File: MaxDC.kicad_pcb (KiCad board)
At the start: 2 copper layers, 100 x 100 mm, 34 parts, among them J1 Screw_Terminal_01x03, J2 Screw_Terminal_01x04, T2 70063K

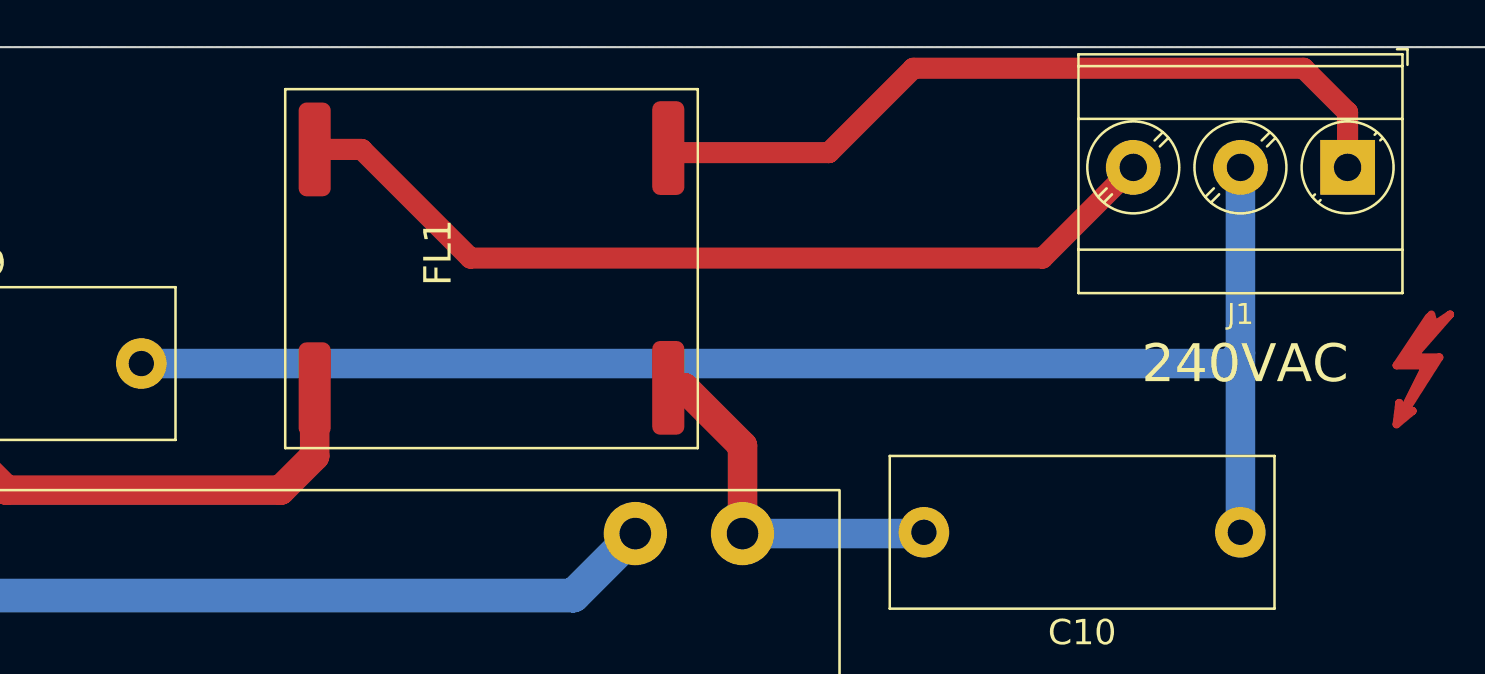
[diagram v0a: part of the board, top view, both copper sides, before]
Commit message: Add files via upload
Begin Changes for creepage.   Reverse N and E input terminals.
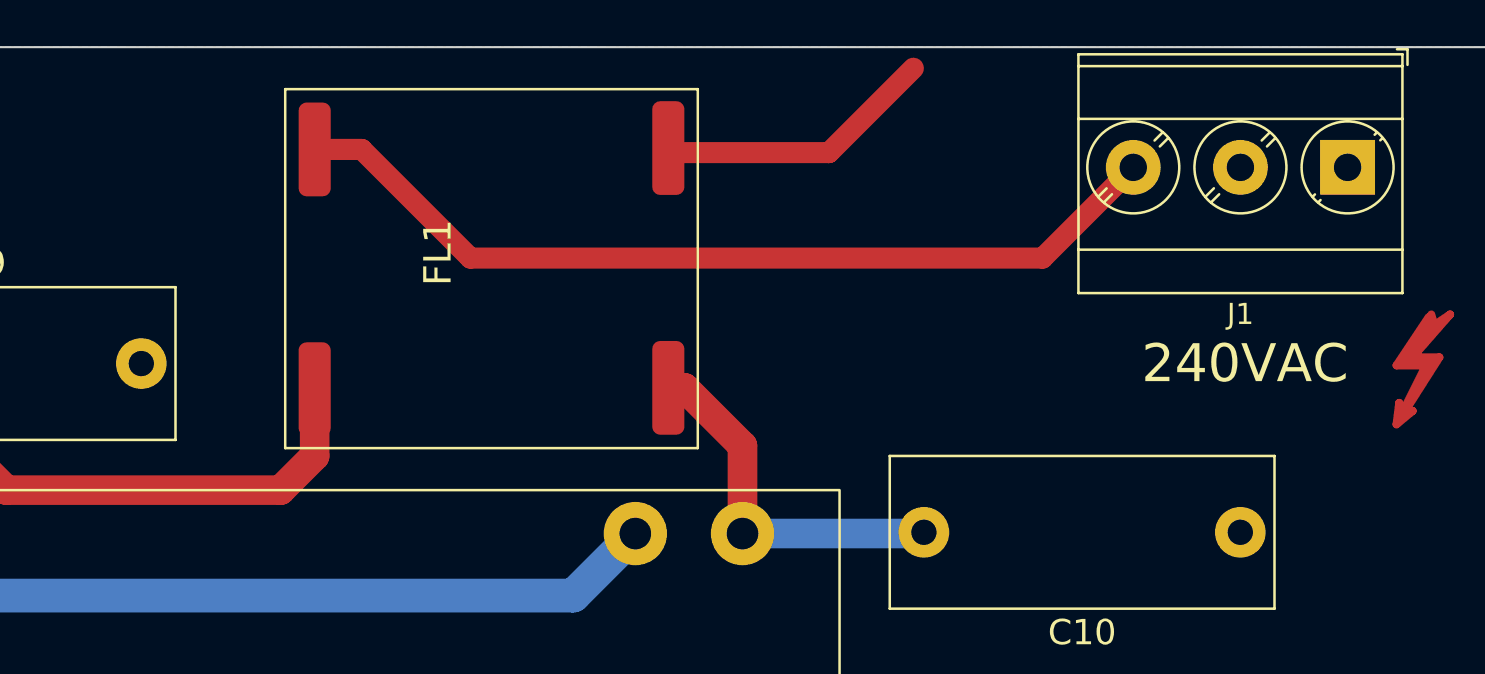
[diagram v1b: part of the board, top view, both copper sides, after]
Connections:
- J1 pad 1: Net-(FL1-Pad4) -> Earth_Protective
- J1 pad 2: Earth_Protective -> Net-(FL1-Pad4)
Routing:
- net Earth_Protective: track 69.6 -> 0.01 mm
- net Net-(FL1-Pad4): track 37.4 -> 13.4 mm
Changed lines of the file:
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@@
     (fp_circle (center 0 0) (end 2 0) (layer "F.Fab") (width 0.1) (fill none))
     (pad "1" thru_hole rect (at 0 0 180) (size 2.6 2.6) (drill 1.3) (layers *.Cu *.Mask)
-      (net 6 "Net-(FL1-Pad4)") (pinfunction "Pin_1") (pintype "passive"))
+      (net 7 "Earth_Protective") (pinfunction "Pin_1") (pintype "passive"))
     (pad "2" thru_hole circle (at 5.08 0 180) (size 2.6 2.6) (drill 1.3) (layers *.Cu *.Mask)
-      (net 7 "Earth_Protective") (pinfunction "Pin_2") (pintype "passive"))
+      (net 6 "Net-(FL1-Pad4)") (pinfunction "Pin_2") (pintype "passive"))
     (pad "3" thru_hole circle (at 10.16 0 180) (size 2.6 2.6) (drill 1.3) (layers *.Cu *.Mask)
       (net 8 "Net-(FL1-Pad1)") (pinfunction "Pin_3") (pintype "passive"))
@@
   (segment (start 105.1 73.06) (end 105.1 67.9) (width 1.4) (layer "B.Cu") (net 5))
   (segment (start 105.1 67.9) (end 108 65) (width 1.4) (layer "B.Cu") (net 5))
-  (segment (start 182.5 51) (end 164 51) (width 1) (layer "F.Cu") (net 6))
   (segment (start 160 55) (end 152.597 55) (width 1) (layer "F.Cu") (net 6))
-  (segment (start 184.585 55.7) (end 184.585 53.085) (width 1) (layer "F.Cu") (net 6))
   (segment (start 152.597 55) (end 152.382 54.785) (width 1) (layer "F.Cu") (net 6))
-  (segment (start 184.585 53.085) (end 182.5 51) (width 1) (layer "F.Cu") (net 6))
   (segment (start 164 51) (end 160 55) (width 1) (layer "F.Cu") (net 6))
-  (segment (start 179.505 55.7) (end 179.505 64.495) (width 1.4) (layer "B.Cu") (net 7))
   (segment (start 179.505 72.995) (end 179.5 73) (width 1.4) (layer "B.Cu") (net 7))
-  (segment (start 179.505 64.495) (end 179.505 72.995) (width 1.4) (layer "B.Cu") (net 7))
-  (segment (start 179 65) (end 179.505 64.495) (width 1.4) (layer "B.Cu") (net 7))
-  (segment (start 127.4 65) (end 179 65) (width 1.4) (layer "B.Cu") (net 7))
   (segment (start 143 60) (end 137.8485 54.8485) (width 1) (layer "F.Cu") (net 8))
   (segment (start 137.8485 54.8485) (end 135.618 54.8485) (width 1) (layer "F.Cu") (net 8))

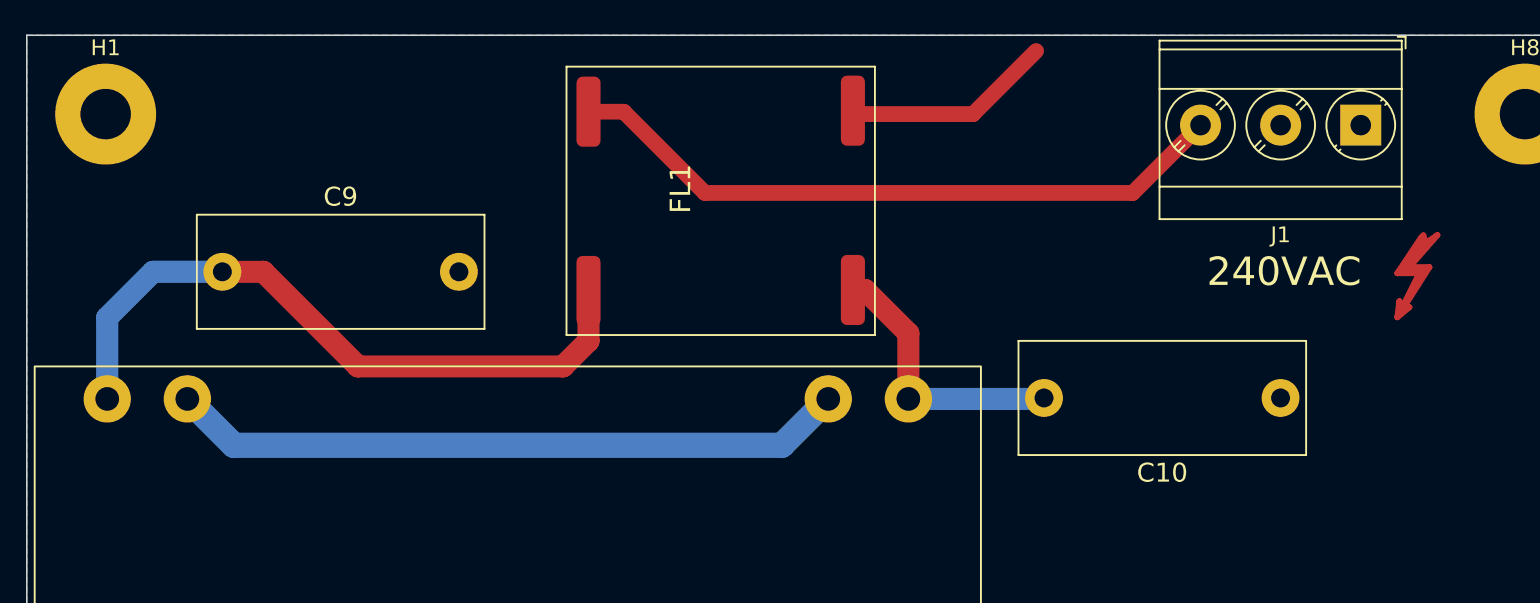
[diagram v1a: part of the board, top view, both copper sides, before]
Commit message: Add files via upload
Adjust placement and spacing for 240VAC safety.   Slots not needed.
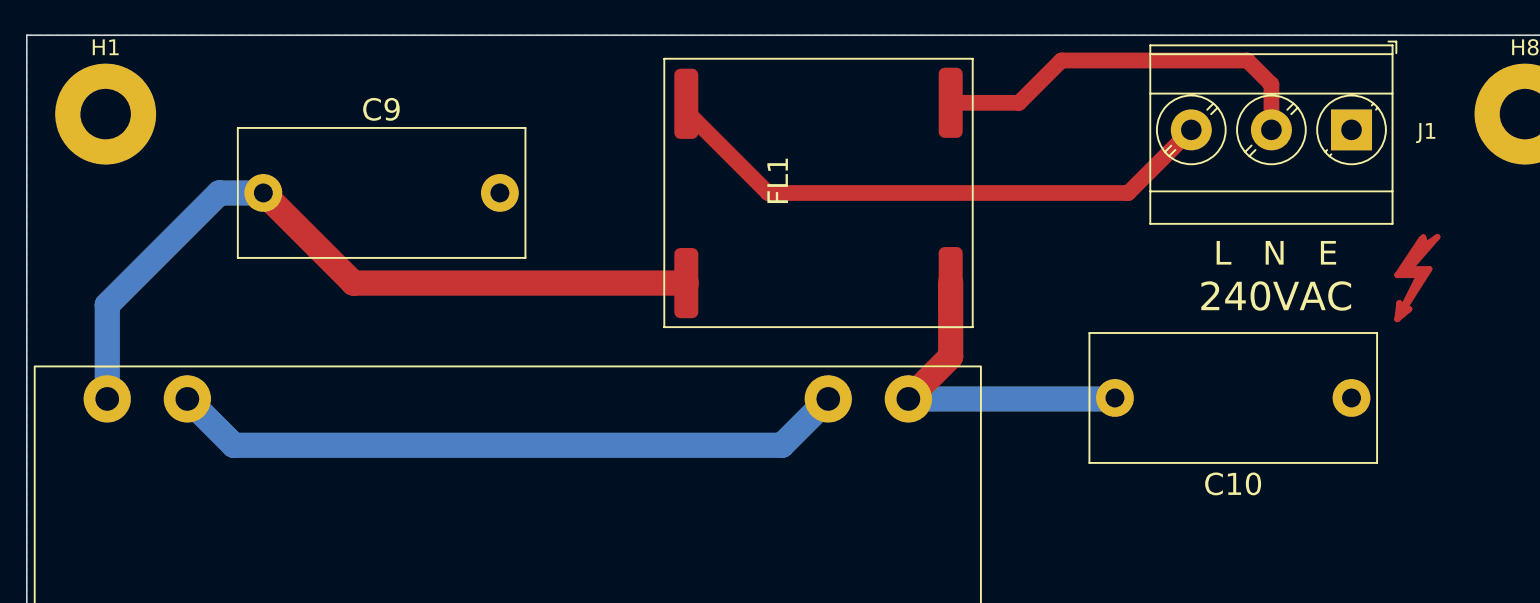
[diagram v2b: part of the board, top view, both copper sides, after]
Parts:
- 240VAC: value Symbol_Highvoltage_Type1_CopperTop_Small -> Symbol_HV_Type1_CopperTop_Small
- C10, C9: footprint Capacitor_THT:C_Rect_L18.0mm_W7.0mm_P15.00mm_FKS3_FKP3 -> Capacitor_THT:C_Rect_L18.0mm_W8.0mm_P15.00mm_FKS3_FKP3
- J1: value Screw_Terminal_01x03 -> L N E
- moved FL1 6.22 mm to (150.2, 60.0)
- moved C9 5.64 mm to (115.0, 60.0)
- moved C10 4.50 mm to (184.0, 73.0)
- moved J1 0.66 mm to (184.0, 56.0)
- moved 240VAC 0.12 mm to (187.3, 66.0)
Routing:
- net Net-(FL1-Pad4): track 13.4 -> 25.0 mm
- net Net-(FL1-Pad1): track 42.7 -> 36.3 mm
- net Net-(C9-Pad1): track 43.3 -> 48.0 mm
- net Net-(C10-Pad2): track 17.4 -> 21.6 mm
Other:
- board text added: "MaxDC 0.2 Andrew Fischer 24012023 License: Creative Commons CC BY-NC 4.0 creativecommons.org/licenses/by-nc/4.0/"
- board text removed: "MaxDC 0.2 Andrew Fischer 22012023 License: Creative Commons CC BY-NC 4.0 creativecommons.org/licenses/by-nc/4.0/"

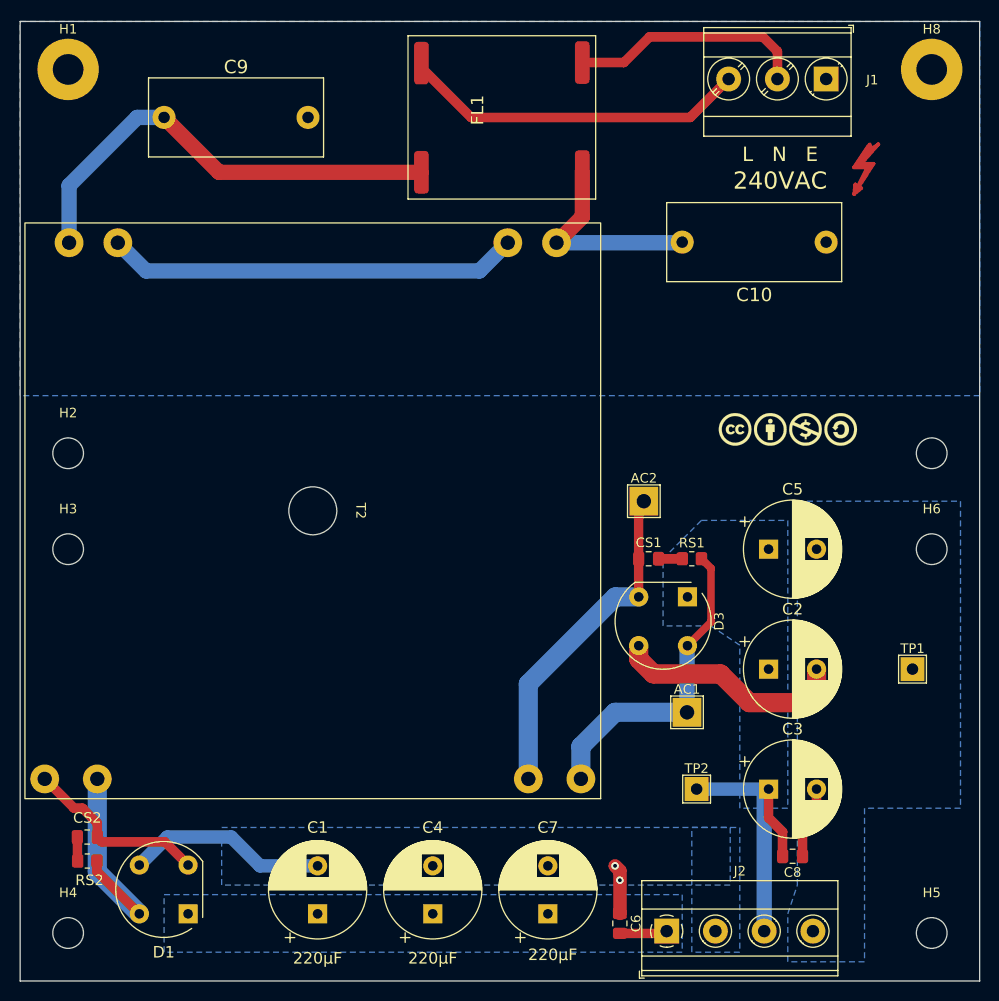
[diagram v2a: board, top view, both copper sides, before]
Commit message: Add files via upload
Uploaded to JLC.   Branch ready to merge back to main.
Move edge to the left and change width to 99.5mm.   After checking a 100mm board in a 1455 case, I made this board .5mm wider.   Move the edges to give the transformer a little more clearance. 
Moved the caps at the bottom of the board up 1mm.  That is to give more clearance for output connectors.    5-way binding posts should clear, but this gives a little more leeway.
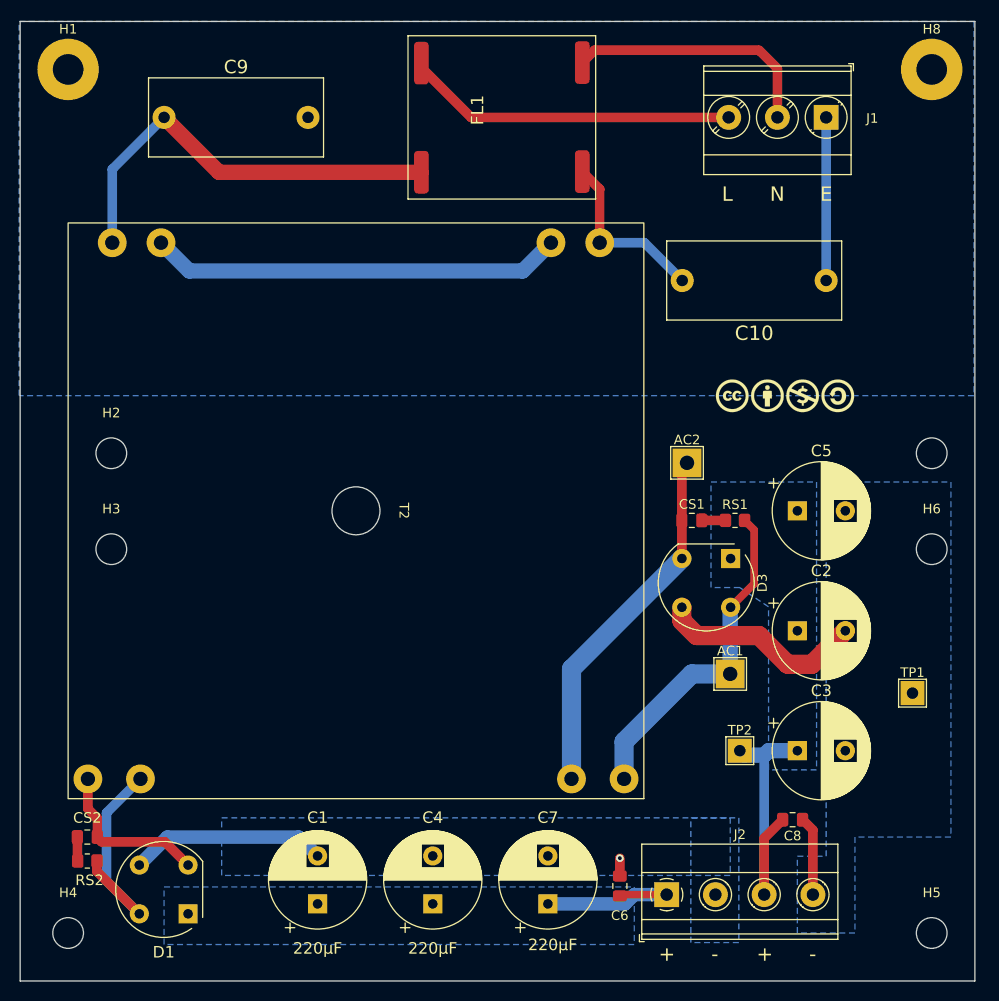
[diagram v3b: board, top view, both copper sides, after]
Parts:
- removed 240VAC: Symbol_HV_Type1_CopperTop_Small, Symbol:Symbol_Highvoltage_Type1_CopperTop_Small
- moved AC1 6.02 mm to (174.0, 118.0)
- moved AC2 6.02 mm to (169.5, 96.0)
- moved CS1 6.02 mm to (170.0, 102.0)
- moved D3 6.02 mm to (174.0, 106.0)
- moved RS1 6.02 mm to (174.5, 102.0)
- moved TP2 6.02 mm to (175.0, 126.0)
- moved C2 5.00 mm to (181.0, 113.5)
- moved C3 5.00 mm to (181.0, 126.0)
- moved C5 5.00 mm to (181.0, 101.0)
- moved H2 4.50 mm to (109.5, 95.0)
- moved H3 4.50 mm to (109.5, 105.0)
- moved T2 4.50 mm to (135.0, 101.0)
- moved C10 4.00 mm to (184.0, 77.0)
- moved J1 4.00 mm to (184.0, 60.0)
- moved C6 3.90 mm to (162.5, 140.1)
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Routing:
- net Earth_Protective: track 0.00 -> 17.0 mm
- net T1: track 4.98 -> 17.7 mm
- net T2: track 26.2 -> 22.5 mm, vias 2 -> 1
- net Net-(C9-Pad1): track 48.0 -> 44.5 mm
- net Net-(C10-Pad2): track 21.6 -> 18.4 mm
- net Net-(AC2-Pad1): track 35.4 -> 37.9 mm
- net Net-(CS2-Pad1): track 19.5 -> 17.2 mm
- net Net-(AC1-Pad1): track 33.4 -> 35.3 mm
- net Net-(FL1-Pad4): track 25.0 -> 26.7 mm
- net T4: track 31.8 -> 30.0 mm
- net Net-(FL1-Pad1): track 36.3 -> 34.6 mm
- net Net-(D1-Pad4): track 23.2 -> 24.3 mm
- net T3: track 30.1 -> 29.5 mm
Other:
- board size 100 x 100 mm -> 99.5 x 100 mm
- board text added: "+"
- board text added: "-"
- board text added: "E"
- board text added: "L"
- board text added: "MaxDC 0.3 Andrew Fischer 05022023 License: Creative Commons CC BY-NC 4.0 creativecommons.org/licenses/by-nc/4.0/"
- board text added: "N"
- board text removed: "MaxDC 0.2 Andrew Fischer 24012023 License: Creative Commons CC BY-NC 4.0 creativecommons.org/licenses/by-nc/4.0/"
